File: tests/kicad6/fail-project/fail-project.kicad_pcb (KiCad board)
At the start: 2 copper layers, 6 parts, among them P1 CONN_01X02

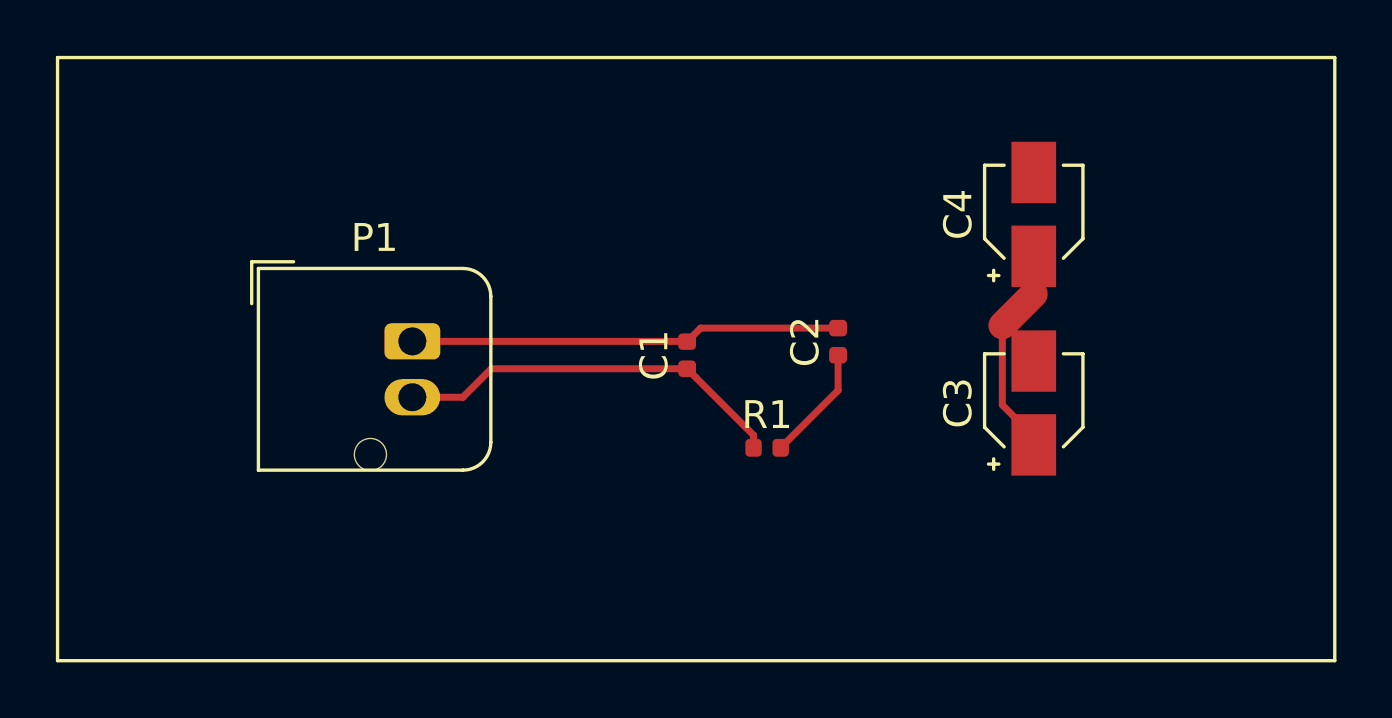
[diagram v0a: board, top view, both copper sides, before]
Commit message: Fixed the PCB edge for v6 fail-project
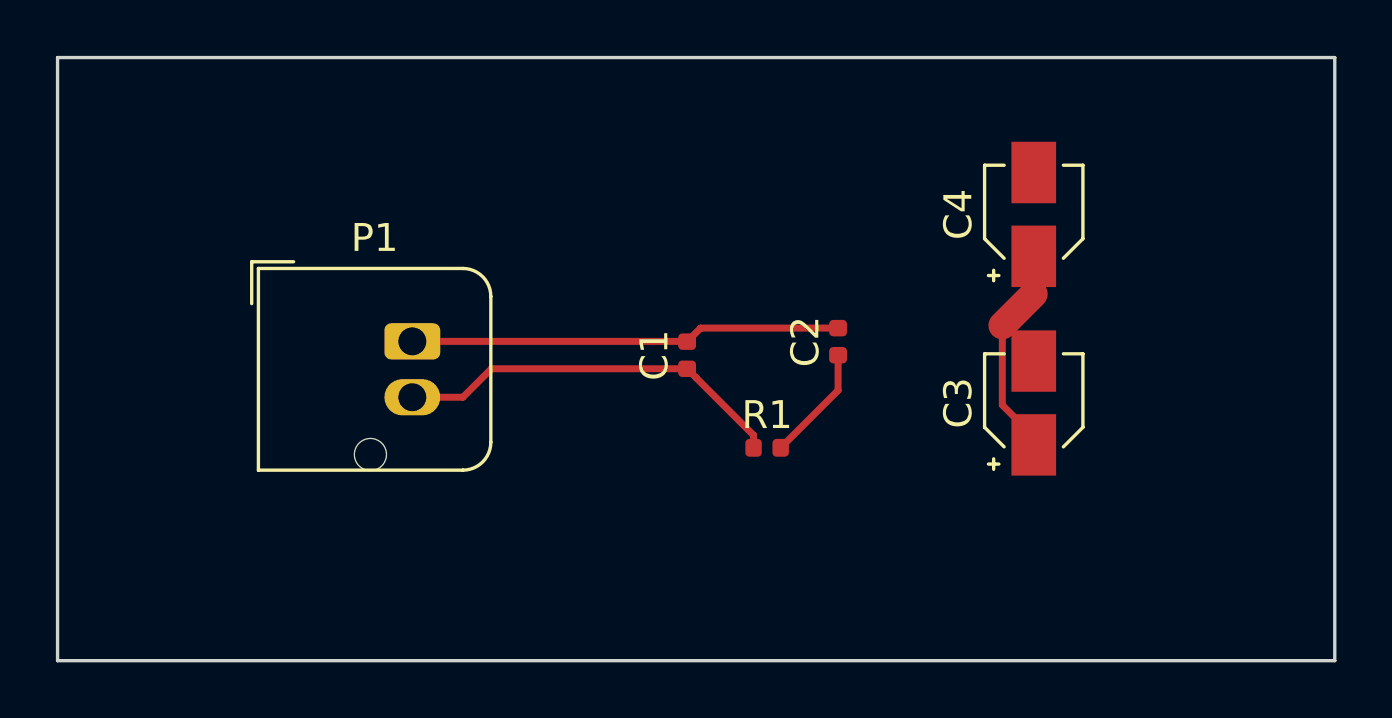
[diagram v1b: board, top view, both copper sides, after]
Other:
- board outline added: 45.7 x 21.6 mm
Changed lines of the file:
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@@
-(kicad_pcb (version 20200913) (generator pcbnew)
+(kicad_pcb (version 20200916) (generator pcbnew)
   (general
     (thickness 1.6)
@@
     )
   )
-  (gr_line (start 187.96 69.85) (end 142.24 69.85) (layer "F.SilkS") (width 0.12))
-  (gr_line (start 142.24 69.85) (end 142.24 91.44) (layer "F.SilkS") (width 0.12))
-  (gr_line (start 187.96 91.44) (end 187.96 69.85) (layer "F.SilkS") (width 0.12))
-  (gr_line (start 142.24 91.44) (end 187.96 91.44) (layer "F.SilkS") (width 0.12))
+  (gr_line (start 187.96 69.85) (end 142.24 69.85) (layer "Edge.Cuts") (width 0.12))
+  (gr_line (start 142.24 69.85) (end 142.24 91.44) (layer "Edge.Cuts") (width 0.12))
+  (gr_line (start 187.96 91.44) (end 187.96 69.85) (layer "Edge.Cuts") (width 0.12))
+  (gr_line (start 142.24 91.44) (end 187.96 91.44) (layer "Edge.Cuts") (width 0.12))
   (segment (start 167.155 83.37) (end 165.1 81.315) (width 0.25) (layer "F.Cu") (net 1))
   (segment (start 167.155 83.82) (end 167.155 83.37) (width 0.25) (layer "F.Cu") (net 1))
